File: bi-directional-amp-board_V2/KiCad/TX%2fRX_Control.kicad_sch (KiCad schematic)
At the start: 22 parts

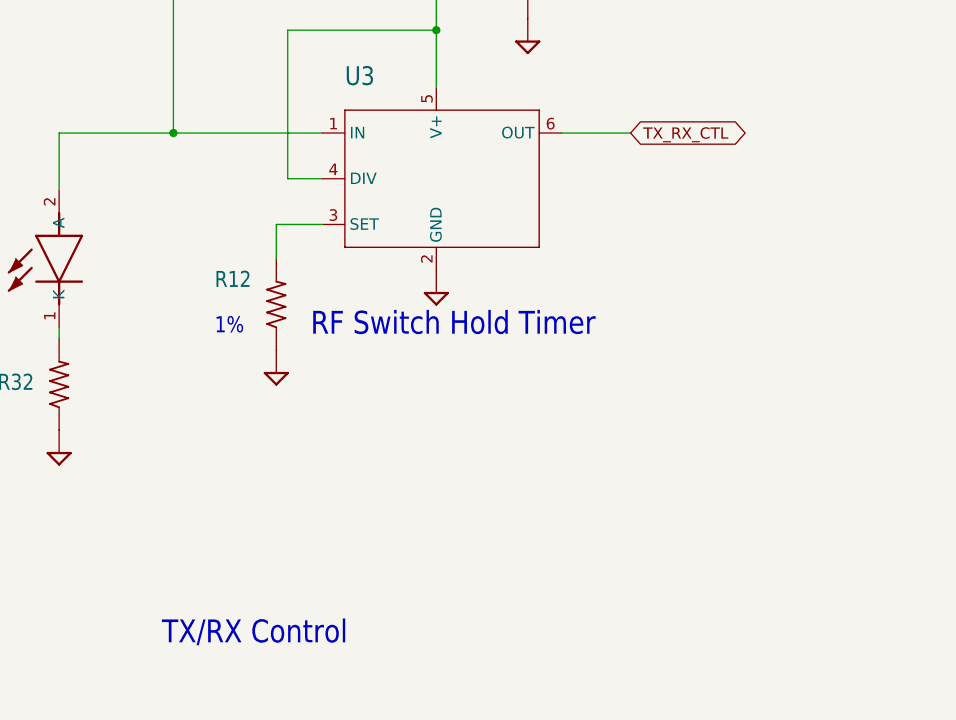
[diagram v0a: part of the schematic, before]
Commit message: re importing eagle files to kicad
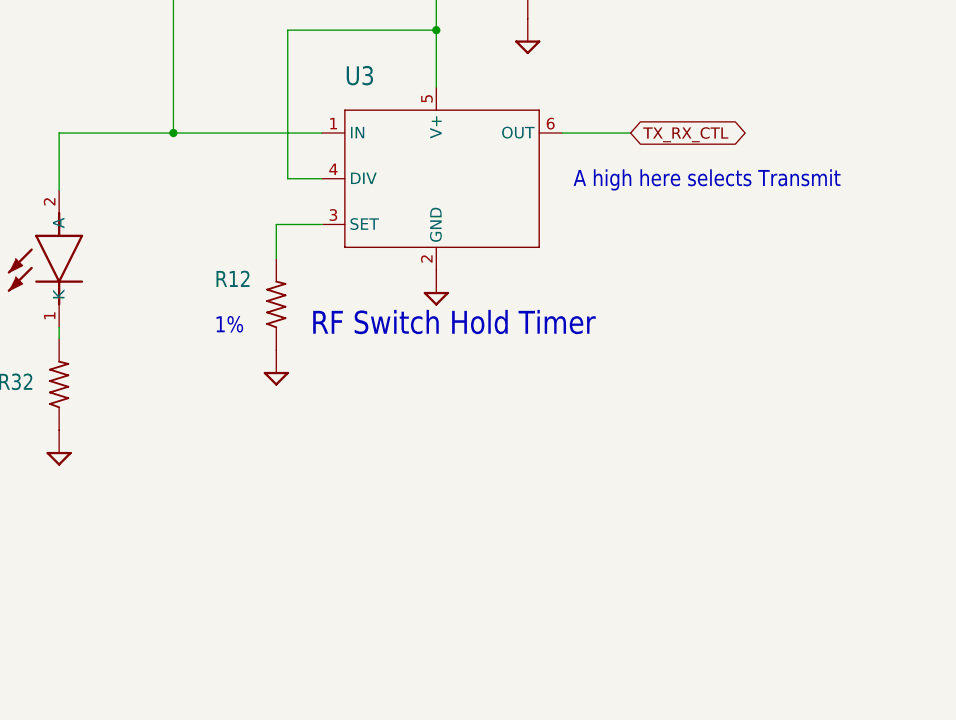
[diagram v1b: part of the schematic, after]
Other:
- note added: "A high here selects Transmit"
- note removed: "TX/RX Control"
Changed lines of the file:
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@@
 (kicad_sch (version 20211123) (generator eeschema)
-  (paper "User" 490.22 254.406)
+  (paper "A2")
   (junction (at 63.5 101.6) (diameter 0) (color 0 0 0 0)
   )
@@
     (effects (font (size 1.778 1.5113)) (justify left bottom))
   )
+  (text "A high here selects Transmit" (at 252.73 157.48 180)
+    (effects (font (size 1.778 1.5113)) (justify left bottom))
+  )
   (text "A high here enables PA" (at 251.46 101.6 180)
     (effects (font (size 1.778 1.5113)) (justify left bottom))
@@
     (effects (font (size 1.778 1.5113)) (justify left bottom))
   )
-  (text "TX/RX Control" (at 207.01 208.28 180)
-    (effects (font (size 2.54 2.159)) (justify left bottom))
-  )
   (text "Standoffs" (at 154.94 208.28 180)

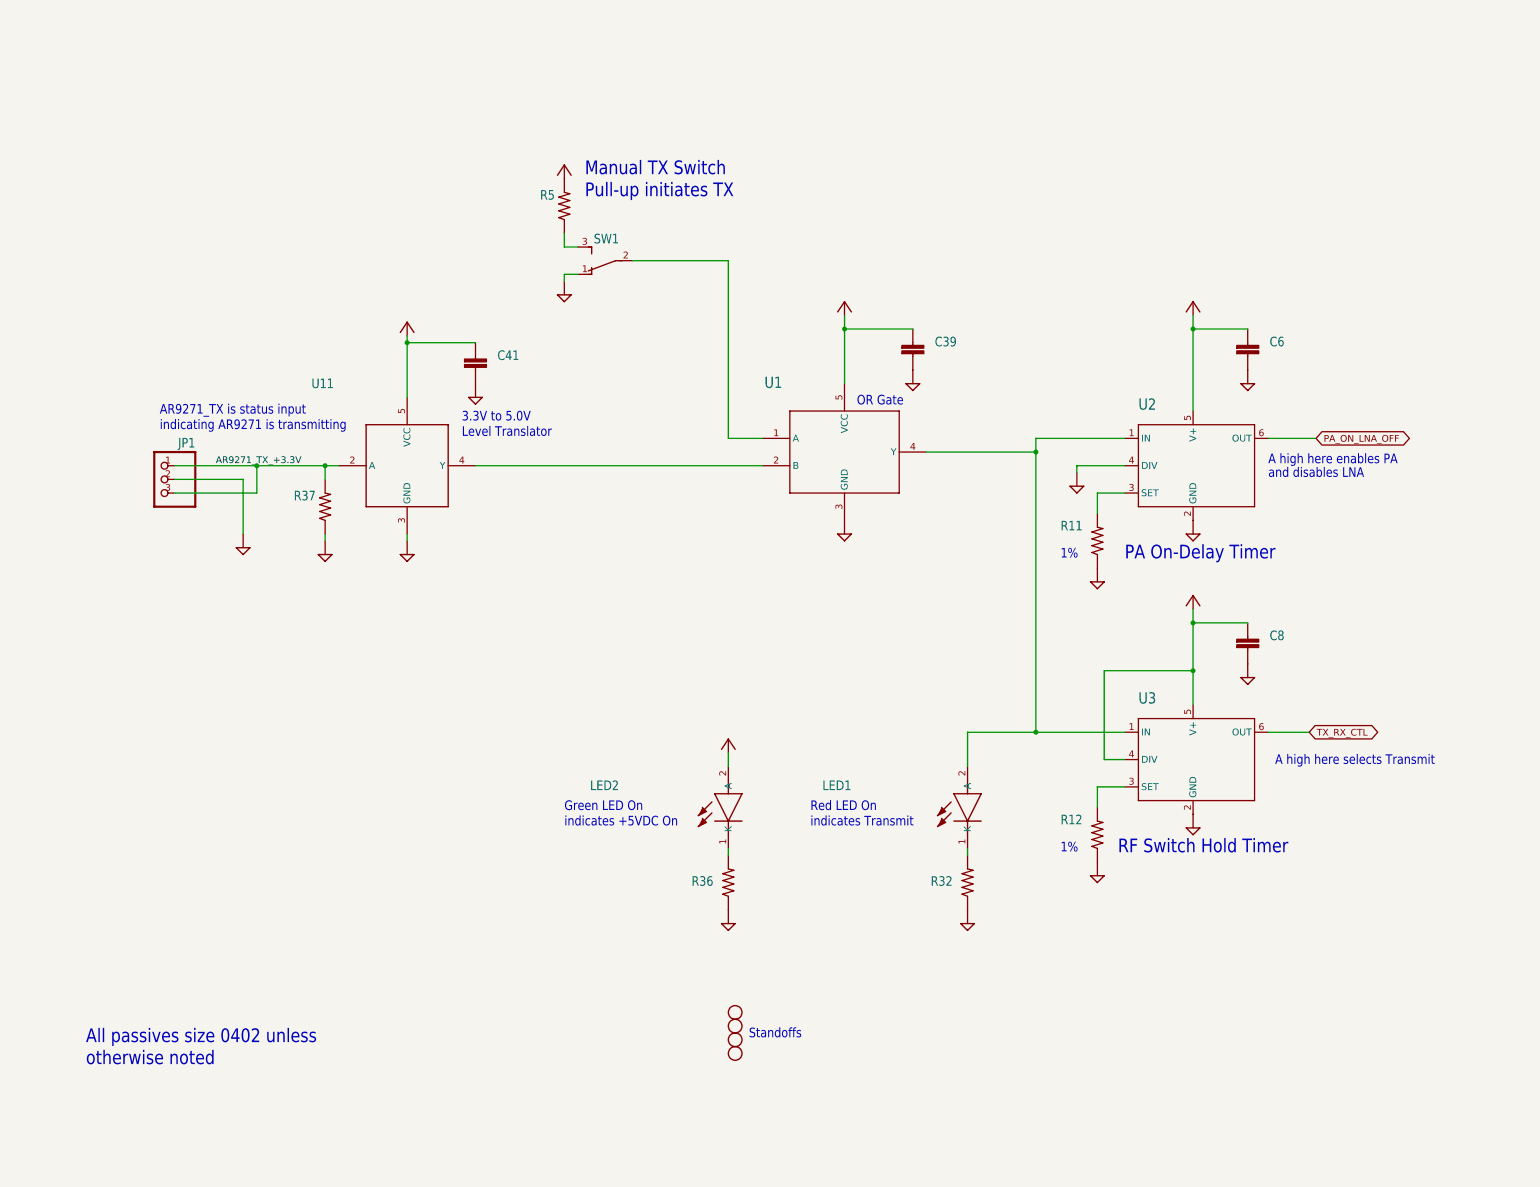
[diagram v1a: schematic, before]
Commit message: Updated KiCAD import of bidirectional amplifier. Still a bit broken, but better now.
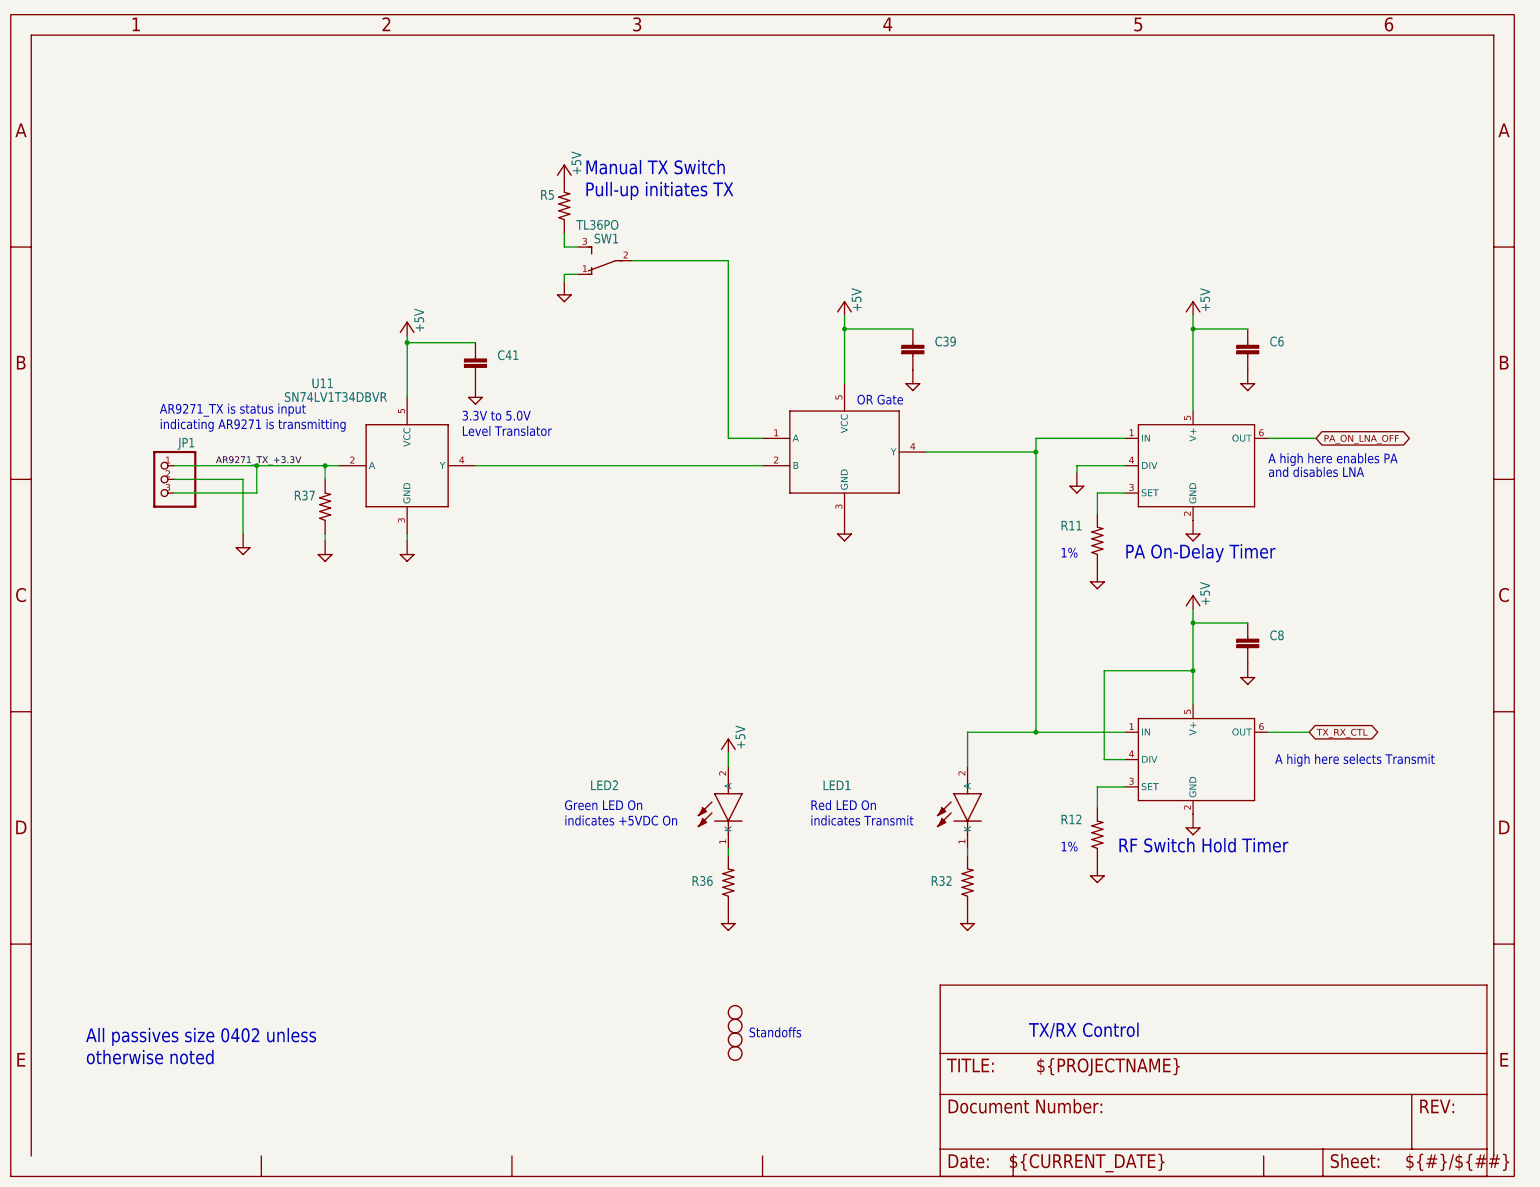
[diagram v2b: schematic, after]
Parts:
- C39, C41, C6, C8: value (none) -> C-EU0402-B-NOSILK; footprint (none) -> Bidirectional_Amp:.0402-B-NOSILK; MFR (none) -> TDK; MPN (none) -> CGA2B1X7R1C104K050BC
- H1, H2, H3, H4: value (none) -> STAND-OFFTIGHT; footprint (none) -> Bidirectional_Amp:STAND-OFF-TIGHT
- JP1: value (none) -> PINHD-1X3; footprint (none) -> Bidirectional_Amp:1X03; MFR (none) -> Molex; MPN (none) -> 22-23-2031
- LED1: value (none) -> LTST-C193KRKT-5A; footprint (none) -> Bidirectional_Amp:LEDC1607X80N
- LED2: value (none) -> LTST-C193KGKT-5A; footprint (none) -> Bidirectional_Amp:LEDC1607X80N
- R11, R12: value (none) -> R-US_0402-B-NOSILK; footprint (none) -> Bidirectional_Amp:.0402-B-NOSILK; MFR (none) -> Panasonic; MPN (none) -> ERJ-2RKF4993X
- R32, R36: value (none) -> R-US_0402-B-NOSILK; footprint (none) -> Bidirectional_Amp:.0402-B-NOSILK; MFR (none) -> Panasonic; MPN (none) -> ERJ-2GEJ102X
- R37, R5: value (none) -> R-US_0402-B-NOSILK; footprint (none) -> Bidirectional_Amp:.0402-B-NOSILK; MFR (none) -> Panasonic; MPN (none) -> ERJ-2GEJ103X
- SW1: value (none) -> TL36PO; footprint (none) -> Bidirectional_Amp:TL3XPO; MFR (none) -> APEM Inc.; MPN (none) -> TL36P005000
- U1: value (none) -> SN74LVC1G32DBVR; footprint (none) -> Bidirectional_Amp:DBV5
- U11: value (none) -> SN74LV1T34DBVR; footprint (none) -> Bidirectional_Amp:SOT95P280X145-5N
- U2, U3: value (none) -> LTC6994-1; footprint (none) -> Bidirectional_Amp:TSOT-23_S6
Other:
- note added: "TX/RX Control"
